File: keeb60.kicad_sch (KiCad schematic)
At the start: 123 parts, among them K000 Esc, K001 1, K002 2, K003 3, K004 4, K005 5, K006 6, K007 7, K008 8, K009 9, K010 0, K011 _, K012 =, K013 Backspace, K100 Tab, K101 Q, K102 W, K103 E, K104 R, K105 T, K106 Y, K107 U, K108 I, K109 O, K110 P, K111 [, K112 ], K113 Pipe, K200 Caps Lock, K201 A, K202 S, K203 D, K204 F, K205 G, K206 H, K207 J, K208 K, K209 L, K210 ;, K211 ,, K213 Enter, K300 Shift, K302 Z, K303 X, K304 C, K305 V, K306 B, K307 N, K308 M, K309 ,, K310 ., K311 /, K313 Shift, K400 Ctrl, K401 Option, K402 Command, K406 Space, K410 Command, K411 Option, K412 Function, K413 Ctrl, U1 ProMicro

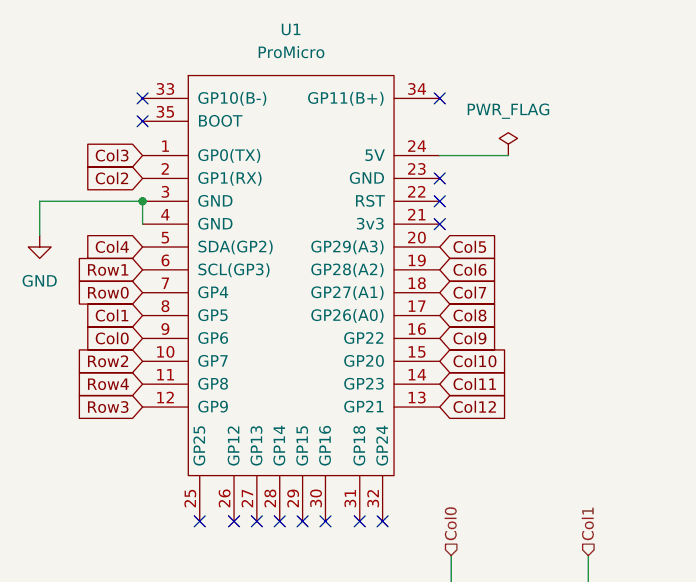
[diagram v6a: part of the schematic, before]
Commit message: Flip nicenano for USB-C access
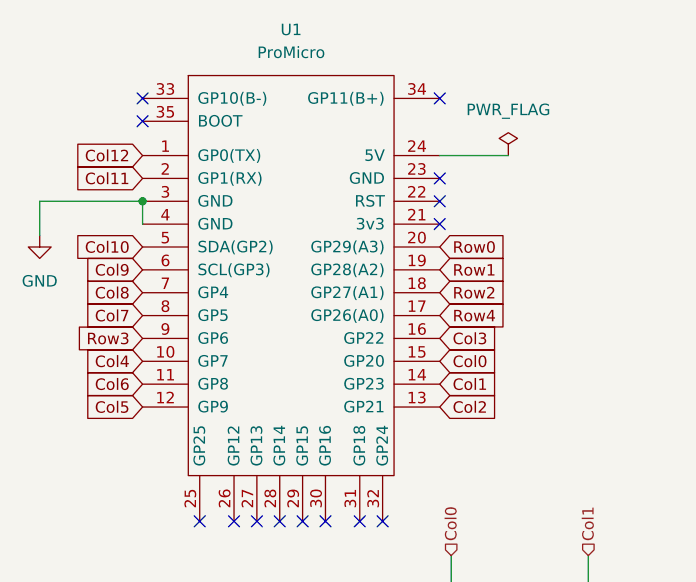
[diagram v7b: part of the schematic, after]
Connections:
- net Col0: now also U1.15 (GP20); no longer U1.9 (GP6)
- net Col1: now also U1.14 (GP23); no longer U1.8 (GP5)
- net Col10: now also U1.5 (SDA(GP2)); no longer U1.15 (GP20)
- net Col11: now also U1.2 (GP1(RX)); no longer U1.14 (GP23)
- net Col12: now also U1.1 (GP0(TX)); no longer U1.13 (GP21)
- net Col2: now also U1.13 (GP21); no longer U1.2 (GP1(RX))
- net Col3: now also U1.16 (GP22); no longer U1.1 (GP0(TX))
- net Col4: now also U1.10 (GP7); no longer U1.5 (SDA(GP2))
- net Col5: now also U1.12 (GP9); no longer U1.20 (GP29(A3))
- net Col6: now also U1.11 (GP8); no longer U1.19 (GP28(A2))
- net Col7: now also U1.8 (GP5); no longer U1.18 (GP27(A1))
- net Col8: now also U1.7 (GP4); no longer U1.17 (GP26(A0))
- net Col9: now also U1.6 (SCL(GP3)); no longer U1.16 (GP22)
- net Row0: now also U1.20 (GP29(A3)); no longer U1.7 (GP4)
- net Row1: now also U1.19 (GP28(A2)); no longer U1.6 (SCL(GP3))
- net Row2: now also U1.18 (GP27(A1)); no longer U1.10 (GP7)
- net Row3: now also U1.9 (GP6); no longer U1.12 (GP9)
- net Row4: now also U1.17 (GP26(A0)); no longer U1.11 (GP8)
